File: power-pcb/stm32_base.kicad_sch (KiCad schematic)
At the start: 41 parts, among them J1 Network Connector, J2 STDC14, SW1 SW_Push, U1 LD39050PU33R, U2 STM32G474RBT6, U3 SN65HVD230, Y1 8MHz

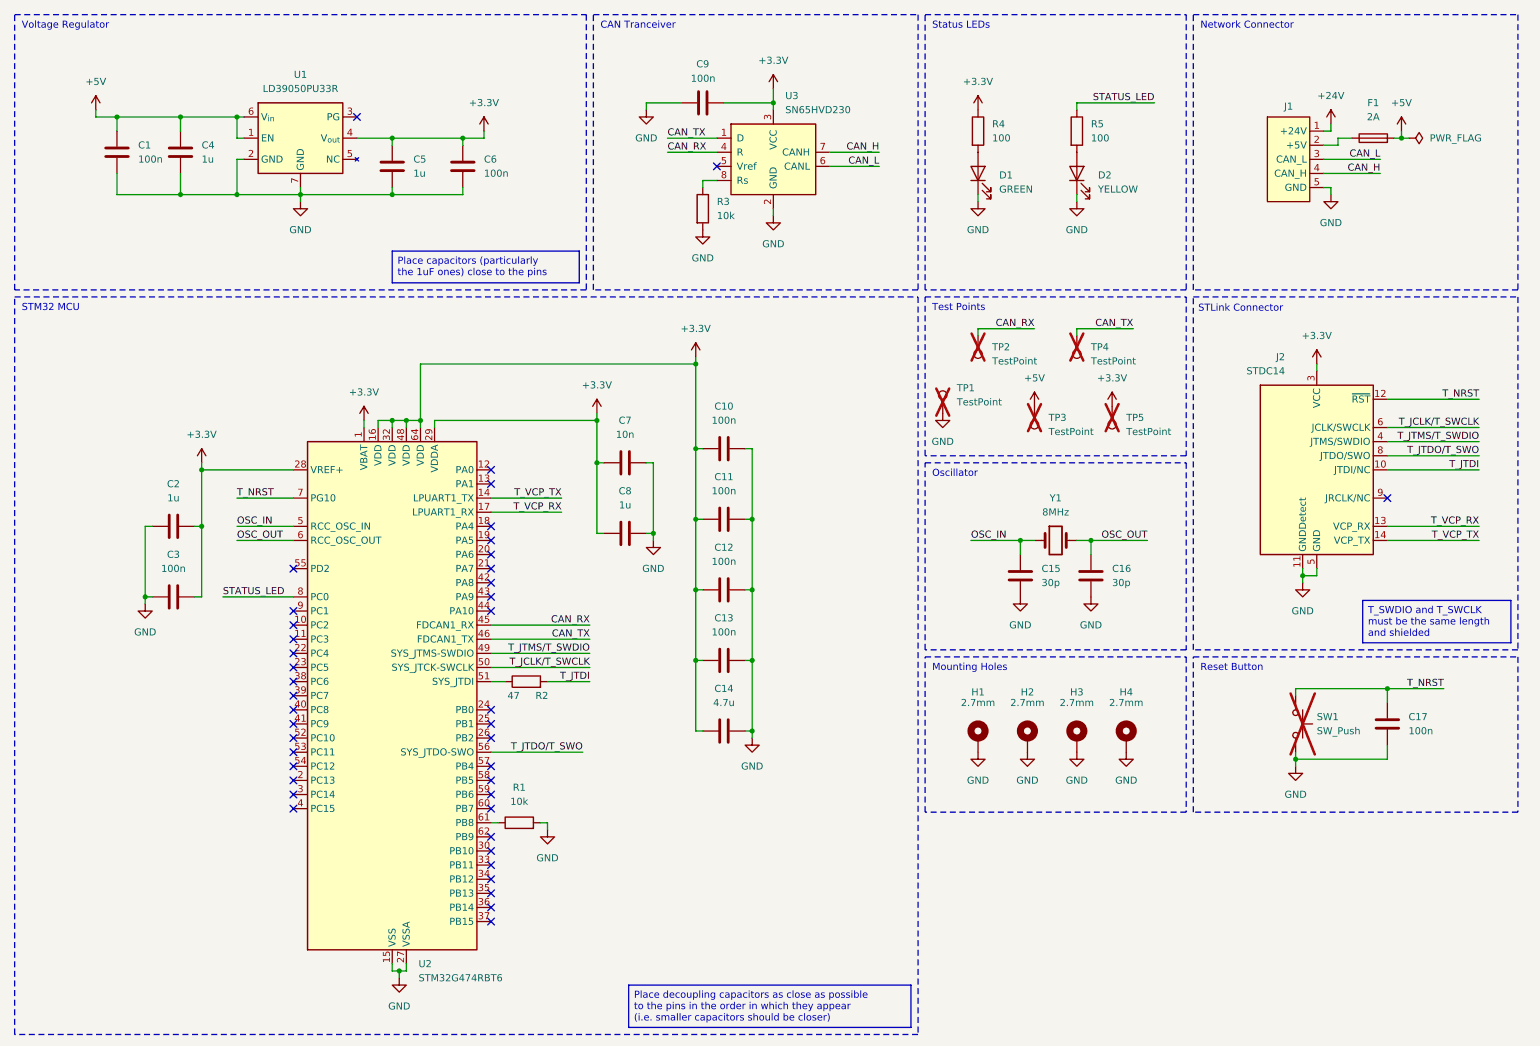
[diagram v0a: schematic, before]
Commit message: power-pcb: complete schematic
Missing some part numbers, footprints and JLCPCB codes.
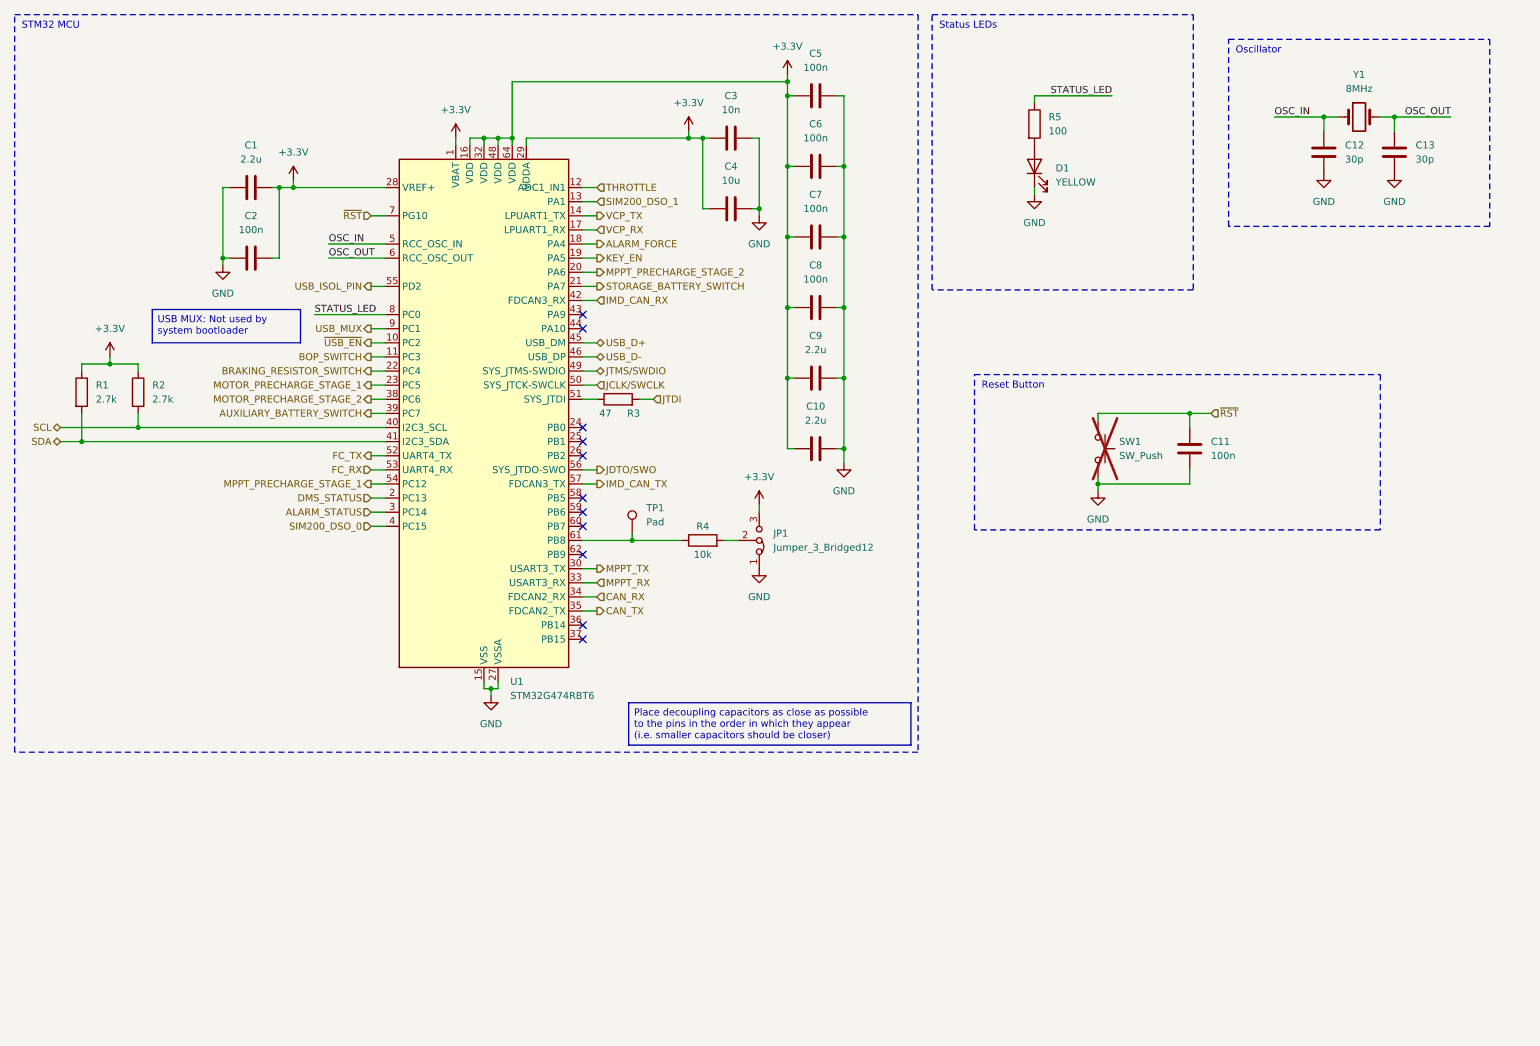
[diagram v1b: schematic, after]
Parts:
- removed C1, C6: 100n, Capacitor_SMD:C_0402_1005Metric, symbol Device:C
- removed C14: 4.7u, Capacitor_SMD:C_0402_1005Metric, symbol Device:C
- removed C4, C5: 1u, Capacitor_SMD:C_0402_1005Metric, symbol Device:C
- removed D1: GREEN, Exocet:LED_0805_2012Metric_With_Annotations, symbol Device:LED
- removed F1: 2A, Exocet:Fuse_Holder_Littelfuse_01530008, symbol Device:Fuse
- removed H1, H2, H3, H4: 2.7mm, MountingHole:MountingHole_2.7mm_Pad, symbol Mechanical:MountingHole_Pad
- removed J1: Network Connector, Connector_Molex:Molex_SPOX_5268-05A_1x05_P2.50mm_Horizontal, symbol Exocet:Network_Connector
- removed J2: STDC14, Connector_PinHeader_1.27mm:PinHeader_2x07_P1.27mm_Vertical_SMD, symbol Connector:Conn_ST_STDC14
- removed R3: 10k, Resistor_SMD:R_0402_1005Metric, symbol Device:R
- removed R4: 100, Resistor_SMD:R_0402_1005Metric, symbol Device:R
- removed TP2, TP3, TP4, TP5: TestPoint, TestPoint:TestPoint_Keystone_5005-5009_Compact, symbol Connector:TestPoint
- removed U1: LD39050PU33R, Package_DFN_QFN:DFN-6-1EP_3x3mm_P0.95mm_EP1.7x2.6mm, symbol Exocet:LD39050PU33R
- removed U3: SN65HVD230, Package_SO:SOIC-8_3.9x4.9mm_P1.27mm, symbol Interface_CAN_LIN:SN65HVD230
- added C10: 2.2u, Capacitor_SMD:C_0805_2012Metric_Pad1.18x1.45mm_HandSolder, symbol Device:C
- added JP1: Jumper_3_Bridged12, symbol Jumper:Jumper_3_Bridged12
- added R1, R2: 2.7k, symbol Device:R
- C1: renamed from C2; value 1u -> 2.2u; footprint Capacitor_SMD:C_0402_1005Metric -> Capacitor_SMD:C_0805_2012Metric_Pad1.18x1.45mm_HandSolder; JLCPCB C52923 -> C377773
- C11: renamed from C17; footprint Capacitor_SMD:C_0402_1005Metric -> Capacitor_SMD:C_0603_1608Metric_Pad1.08x0.95mm_HandSolder; JLCPCB C1525 -> C14663
- C12: renamed from C15; footprint Capacitor_SMD:C_0603_1608Metric -> Capacitor_SMD:C_0603_1608Metric_Pad1.08x0.95mm_HandSolder
- C13: renamed from C16; footprint Capacitor_SMD:C_0603_1608Metric -> Capacitor_SMD:C_0603_1608Metric_Pad1.08x0.95mm_HandSolder
- C2: renamed from C3; footprint Capacitor_SMD:C_0402_1005Metric -> Capacitor_SMD:C_0603_1608Metric_Pad1.08x0.95mm_HandSolder; JLCPCB C1525 -> C14663
- C3: renamed from C7; footprint Capacitor_SMD:C_0402_1005Metric -> Capacitor_SMD:C_0603_1608Metric_Pad1.08x0.95mm_HandSolder; JLCPCB C15195 -> C57112
- C4: renamed from C8; value 1u -> 10u; footprint Capacitor_SMD:C_0402_1005Metric -> Capacitor_SMD:C_1206_3216Metric_Pad1.33x1.80mm_HandSolder; JLCPCB C52923 -> C13585
- C5: renamed from C10; footprint Capacitor_SMD:C_0402_1005Metric -> Capacitor_SMD:C_0603_1608Metric_Pad1.08x0.95mm_HandSolder; JLCPCB C1525 -> C14663
- C6: renamed from C11; footprint Capacitor_SMD:C_0402_1005Metric -> Capacitor_SMD:C_0603_1608Metric_Pad1.08x0.95mm_HandSolder; JLCPCB C1525 -> C14663
- C7: renamed from C12; footprint Capacitor_SMD:C_0402_1005Metric -> Capacitor_SMD:C_0603_1608Metric_Pad1.08x0.95mm_HandSolder; JLCPCB C1525 -> C14663
- C8: renamed from C13; footprint Capacitor_SMD:C_0402_1005Metric -> Capacitor_SMD:C_0603_1608Metric_Pad1.08x0.95mm_HandSolder; JLCPCB C1525 -> C14663
- C9: value 100n -> 2.2u; footprint Capacitor_SMD:C_0402_1005Metric -> Capacitor_SMD:C_0805_2012Metric_Pad1.18x1.45mm_HandSolder; JLCPCB C1525 -> C377773
- TP1: value TestPoint -> Pad; footprint TestPoint:TestPoint_Keystone_5005-5009_Compact -> (none); Net Label GND -> (none); now fitted
- renumbered D2 to D1, R2 to R3, R1 to R4, U2 to U1
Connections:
- net +3.3V: now also C10.1, JP1.3 (B), R1.1, R2.1
- net CAN_RX: now also U1.34 (PB12); no longer U1.45 (PA11)
- net CAN_TX: now also U1.35 (PB13); no longer U1.46 (PA12)
- net GND: now also C10.2, JP1.1 (A); no longer R4.2, TP1.1
- net ~{USB_EN}: now reaches U1.10 (PC2)
- net BOP_SWITCH: now reaches U1.11 (PC3)
- net THROTTLE: now reaches U1.12 (PA0)
- net SIM200_DSO_1: now reaches U1.13 (PA1)
- net ALARM_FORCE: now reaches U1.18 (PA4)
- net KEY_EN: now reaches U1.19 (PA5)
- net DMS_STATUS: now reaches U1.2 (PC13)
- net MPPT_PRECHARGE_STAGE_2: now reaches U1.20 (PA6)
- net STORAGE_BATTERY_SWITCH: now reaches U1.21 (PA7)
- net BRAKING_RESISTOR_SWITCH: now reaches U1.22 (PC4)
- net MOTOR_PRECHARGE_STAGE_1: now reaches U1.23 (PC5)
- net ALARM_STATUS: now reaches U1.3 (PC14)
- net MPPT_TX: now reaches U1.30 (PB10)
- net MPPT_RX: now reaches U1.33 (PB11)
- net MOTOR_PRECHARGE_STAGE_2: now reaches U1.38 (PC6)
- net AUXILIARY_BATTERY_SWITCH: now reaches U1.39 (PC7)
- net SIM200_DSO_0: now reaches U1.4 (PC15)
- net SCL: now reaches U1.40 (PC8)
- net SCL: now also R2.2
- net SDA: now reaches U1.41 (PC9)
- net SDA: now also R1.2
- net IMD_CAN_RX: now reaches U1.42 (PA8)
- net FC_TX: now reaches U1.52 (PC10)
- net FC_RX: now reaches U1.53 (PC11)
- net MPPT_PRECHARGE_STAGE_1: now reaches U1.54 (PC12)
- net USB_ISOL_PIN: now reaches U1.55 (PD2)
- net IMD_CAN_TX: now reaches U1.57 (PB4)
- net at R4.1, U1.61 (PB8): now also TP1.1
- net USB_MUX: now reaches U1.9 (PC1)
- net T_JCLK/T_SWCLK renamed JCLK/SWCLK
- net T_JTDI renamed JTDI
- net T_JTDO/T_SWO renamed JDTO/SWO
- net T_JTMS/T_SWDIO renamed JTMS/SWDIO
- net T_NRST renamed ~{RST}
- net T_VCP_RX renamed VCP_RX
- net T_VCP_TX renamed VCP_TX
- new net: JP1.2 (C), R4.2
- new net USB_D+: U1.45 (PA11)
- new net USB_D-: U1.46 (PA12)
- no-connect marks 42 -> 11
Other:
- note removed: "CAN Tranceiver"
- note removed: "Mounting Holes"
- note removed: "Network Connector"
- note removed: "STLink Connector"
- note removed: "Test Points"
- note removed: "Voltage Regulator"
- title: STM32 Base Layout -> STM32 Microcontroller
- moved on the sheet: C1, C11, C12, C13, C2, C3, C4, C5, C6, C7, C8, D1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

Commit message: power-pcb: finish schematic pages 1 to 7
- overview
- non-isolated interfaces + power
- stm32 microcontroller
- relay board connection
- battery sensors
- 48v i-v sensing (x2)
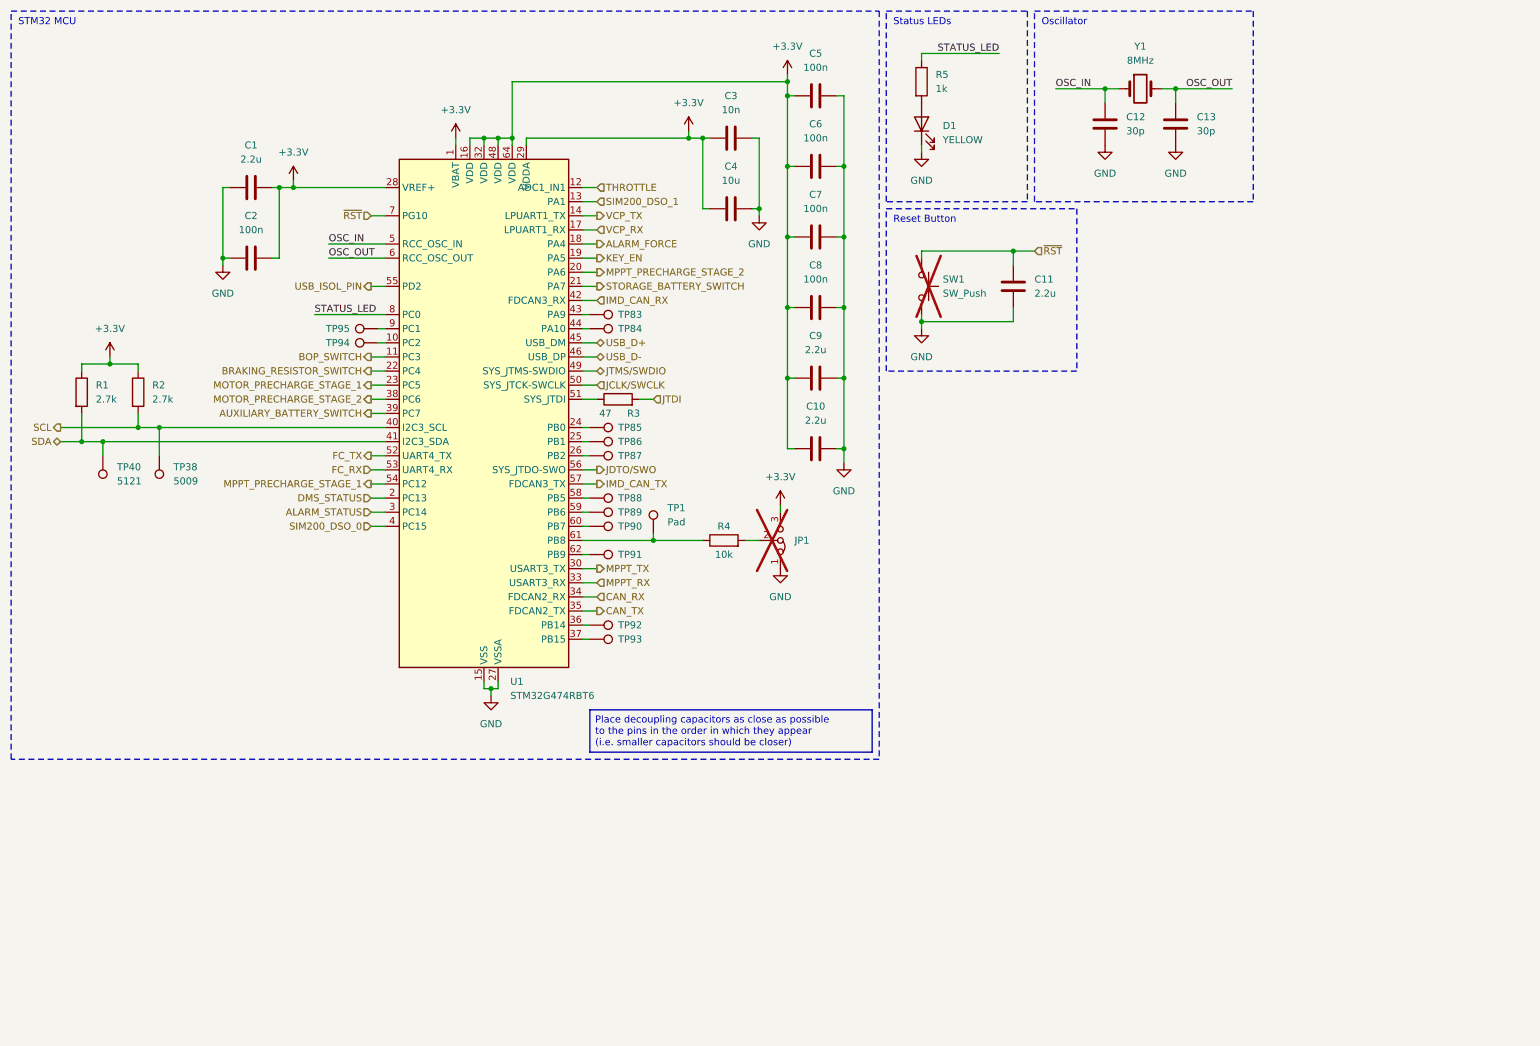
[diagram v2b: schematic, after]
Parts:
- added TP38: 5009, symbol Connector:TestPoint
- added TP40: 5121, symbol Connector:TestPoint
- added TP83, TP84, TP85, TP86, TP87, TP88, TP89, TP90, TP91, TP92, TP93, TP94, TP95: TestPoint, TestPoint:TestPoint_THTPad_D2.0mm_Drill1.0mm, symbol Connector:TestPoint
- C11: value 100n -> 2.2u; footprint Capacitor_SMD:C_0603_1608Metric_Pad1.08x0.95mm_HandSolder -> (none); JLCPCB C14663 -> (none)
- JP1: now not fitted; now in the parts list
- R5: value 100 -> 1k; footprint Resistor_SMD:R_0402_1005Metric -> (none); JLCPCB C25076 -> (none)
- TP1: now left out of the parts list
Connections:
- net SCL: now also TP38.1
- net SDA: now also TP40.1
- net at U1.24 (PB0): now also TP85.1
- net at U1.25 (PB1): now also TP86.1
- net at U1.26 (PB2): now also TP87.1
- net at U1.36 (PB14): now also TP92.1
- net at U1.37 (PB15): now also TP93.1
- net at U1.43 (PA9): now also TP83.1
- net at U1.44 (PA10): now also TP84.1
- net at U1.58 (PB5): now also TP88.1
- net at U1.59 (PB6): now also TP89.1
- net at U1.60 (PB7): now also TP90.1
- net at U1.62 (PB9): now also TP91.1
- net USB_MUX: no longer names the net of U1.9 (PC1)
- net USB_MUX: now also TP95.1
- net ~{USB_EN}: no longer names the net of U1.10 (PC2)
- net ~{USB_EN}: now also TP94.1
- no-connect marks 11 -> 0
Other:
- moved on the sheet: C11, C12, C13, D1, R4, R5, SW1, TP1, Y1
